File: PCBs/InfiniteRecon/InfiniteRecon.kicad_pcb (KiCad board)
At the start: 4 copper layers, 64 parts, among them J1 USB_C_Receptacle, U1 BQ25185DLHR, U2 MAX17048G_T10, U3 TPS62842DGRR, U4 TPS22918TDBVRQ1, U5 ESP32-S3-WROOM-1, U6 TPL5010DDCR, U7 PCMD3180IRTWR

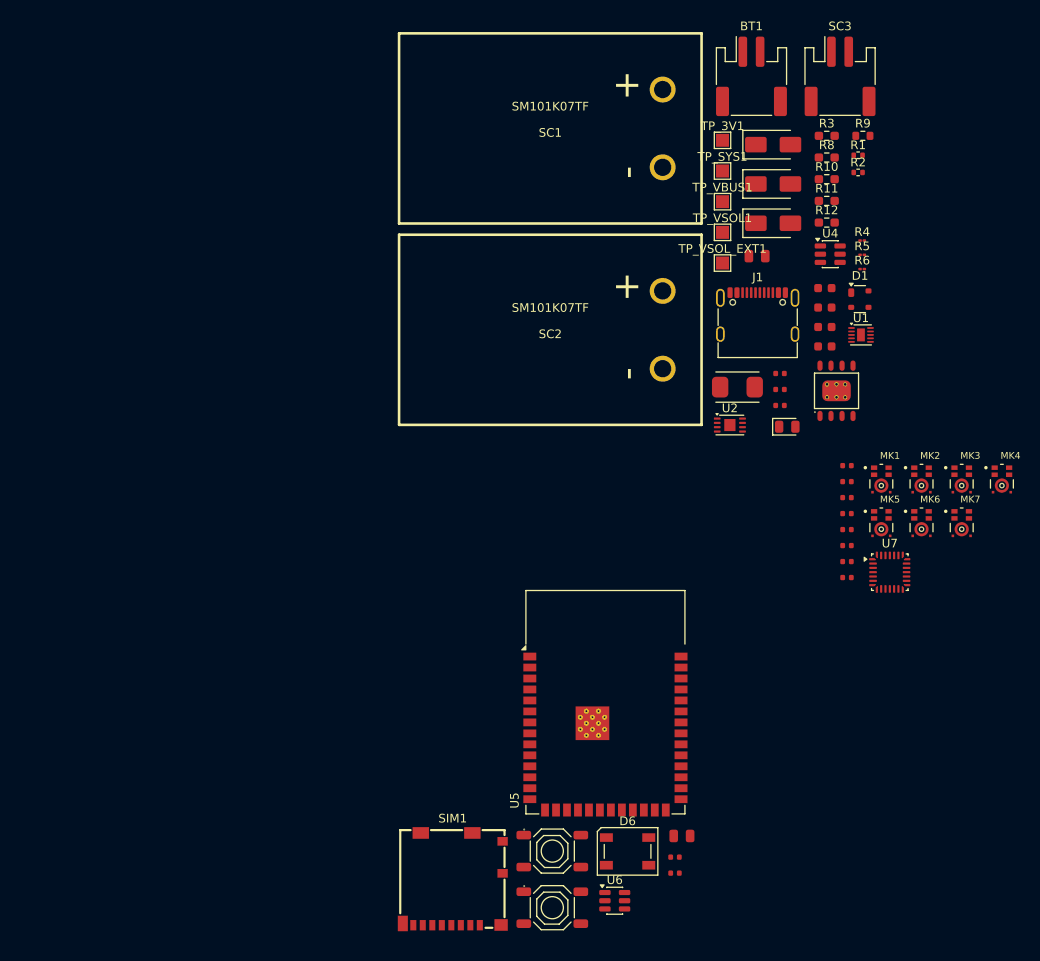
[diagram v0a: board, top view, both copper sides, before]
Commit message: Fixed footprints and some not connected caps
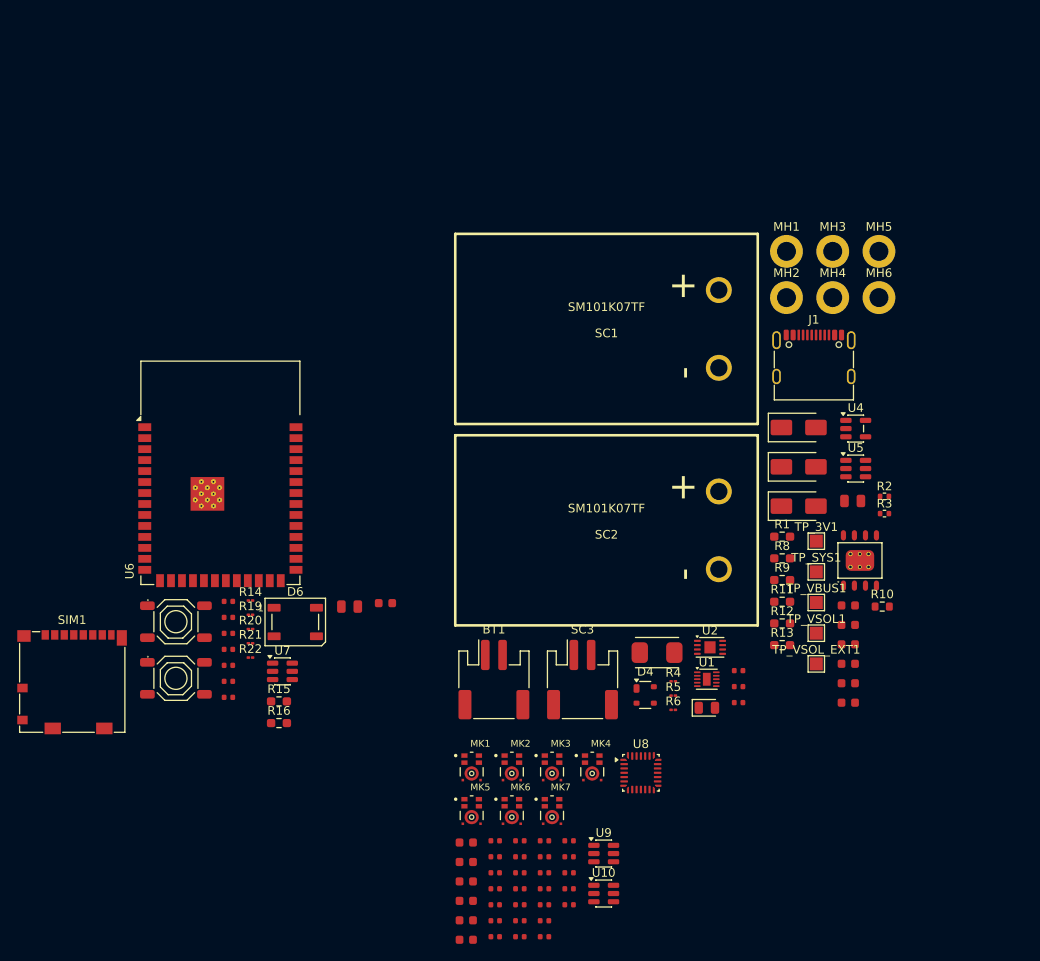
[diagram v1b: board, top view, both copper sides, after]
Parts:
- added C17: 0.1uF, PCM_JLCPCB:C_0402, F.Cu at (156.2, 134.7)
- added C18: 0.1uF, PCM_JLCPCB:C_0402, F.Cu at (156.2, 136.6)
- added C21: 0.1uF, PCM_JLCPCB:C_0402, F.Cu at (156.2, 142.1)
- added C22: 0.1uF, PCM_JLCPCB:C_0402, F.Cu at (156.2, 144.0)
- added C23: 0.1uF, PCM_JLCPCB:C_0402, F.Cu at (156.2, 145.8)
- added C24: 0.1uF, PCM_JLCPCB:C_0402, F.Cu at (159.1, 134.7)
- added C25: 0.1uF, PCM_JLCPCB:C_0402, F.Cu at (159.1, 136.6)
- added C26: 0.1uF, PCM_JLCPCB:C_0402, F.Cu at (159.1, 138.4)
- added C27: 0.1uF, PCM_JLCPCB:C_0402, F.Cu at (159.1, 140.3)
- added C28: 0.1uF, PCM_JLCPCB:C_0402, F.Cu at (159.1, 142.1)
- added C29: 10uF, PCM_JLCPCB:C_0603, F.Cu at (152.9, 134.9)
- added C30: 0.1uF, PCM_JLCPCB:C_0402, F.Cu at (159.1, 144.0)
- added C31: 1uF, PCM_JLCPCB:C_0603, F.Cu at (152.9, 137.2)
- added C32: 1uF, PCM_JLCPCB:C_0603, F.Cu at (152.9, 139.4)
- added C33: 1uF, PCM_JLCPCB:C_0603, F.Cu at (152.9, 141.7)
- added C34: 10uF, PCM_JLCPCB:C_0603, F.Cu at (152.9, 143.9)
- added C35: 0.1uF, PCM_JLCPCB:C_0402, F.Cu at (159.1, 145.8)
- added C36: 10uF, PCM_JLCPCB:C_0603, F.Cu at (152.9, 146.2)
- added C37: 0.1uF, PCM_JLCPCB:C_0402, F.Cu at (161.9, 134.7)
- added MH1: MountingHole_Pad, MountingHole:MountingHole_2.2mm_M2_DIN965_Pad, F.Cu at (189.9, 66.5)
- added MH2: MountingHole_Pad, MountingHole:MountingHole_2.2mm_M2_DIN965_Pad, F.Cu at (189.9, 71.9)
- added MH3: MountingHole_Pad, MountingHole:MountingHole_2.2mm_M2_DIN965_Pad, F.Cu at (195.3, 66.5)
- added MH4: MountingHole_Pad, MountingHole:MountingHole_2.2mm_M2_DIN965_Pad, F.Cu at (195.3, 71.9)
- added MH5: MountingHole_Pad, MountingHole:MountingHole_2.2mm_M2_DIN965_Pad, F.Cu at (200.6, 66.5)
- added MH6: MountingHole_Pad, MountingHole:MountingHole_2.2mm_M2_DIN965_Pad, F.Cu at (200.6, 71.9)
- added R13: 0Ω, Resistor_SMD:R_0603_1608Metric_Pad0.98x0.95mm_HandSolder, F.Cu at (189.4, 112.1)
- added R14: 10K, Resistor_SMD:R_01005_0402Metric, F.Cu at (127.9, 106.9)
- added R15: 10K, Resistor_SMD:R_0603_1608Metric_Pad0.98x0.95mm_HandSolder, F.Cu at (131.2, 118.6)
- added R16: 10K, Resistor_SMD:R_0603_1608Metric_Pad0.98x0.95mm_HandSolder, F.Cu at (131.2, 121.1)
- added R17: 20kΩ, PCM_JLCPCB:R_0402, F.Cu at (125.3, 116.3)
- added R18: 100K, PCM_JLCPCB:R_0402, F.Cu at (125.3, 118.1)
- added R19: 10K, Resistor_SMD:R_01005_0402Metric, F.Cu at (127.9, 108.6)
- added R20: 10K, Resistor_SMD:R_01005_0402Metric, F.Cu at (127.9, 110.2)
- added R21: 10K, Resistor_SMD:R_01005_0402Metric, F.Cu at (127.9, 111.9)
- added R22: 10K, Resistor_SMD:R_01005_0402Metric, F.Cu at (127.9, 113.5)
- added R23: 33, PCM_JLCPCB:R_0402, F.Cu at (161.9, 136.6)
- added R24: 33, PCM_JLCPCB:R_0402, F.Cu at (161.9, 138.4)
- added R25: 33, PCM_JLCPCB:R_0402, F.Cu at (161.9, 140.3)
- added R26: 33, PCM_JLCPCB:R_0402, F.Cu at (161.9, 142.1)
- added R27: 33, PCM_JLCPCB:R_0402, F.Cu at (161.9, 144.0)
- added R28: 33, PCM_JLCPCB:R_0402, F.Cu at (161.9, 145.8)
- added R29: 33, PCM_JLCPCB:R_0402, F.Cu at (164.8, 134.7)
- added R30: 33, PCM_JLCPCB:R_0402, F.Cu at (164.8, 136.6)
- added R31: 33, PCM_JLCPCB:R_0402, F.Cu at (164.8, 138.4)
- added R32: 33, PCM_JLCPCB:R_0402, F.Cu at (164.8, 140.3)
- added R33: 33, PCM_JLCPCB:R_0402, F.Cu at (164.8, 142.1)
- added U10: SN74LVC1T45DBV, Package_TO_SOT_SMD:SOT-23-6, F.Cu at (168.8, 140.8)
- added U8: PCMD3180IRTWR, Package_DFN_QFN:QFN-28_4x4mm_P0.5mm, F.Cu at (173.1, 126.9)
- added U9: SN74LVC1T45DBV, Package_TO_SOT_SMD:SOT-23-6, F.Cu at (168.8, 136.2)
- C11: value 0.1uF -> 1uF; footprint PCM_JLCPCB:C_0402 -> PCM_JLCPCB:C_0603
- C13: value 0.1uF -> 22uF; footprint PCM_JLCPCB:C_0402 -> PCM_JLCPCB:C_0805
- C15: value 22uF -> 0.1uF; footprint PCM_JLCPCB:C_0805 -> PCM_JLCPCB:C_0402
- C20: value 10uF -> 0.1uF; footprint PCM_JLCPCB:C_0603 -> PCM_JLCPCB:C_0402
- C6: value 220pF -> 1uF; footprint PCM_JLCPCB:C_0402 -> PCM_JLCPCB:C_0603
- C7: value 0.1uF -> 220pF
- C8, C9: value 0.1uF -> 10uF; footprint PCM_JLCPCB:C_0402 -> PCM_JLCPCB:C_0603
- D1: value PRTR5V0U2X -> SS14; footprint Package_TO_SOT_SMD:SOT-143 -> PCM_JLCPCB:D_SMA
- D4: value SS14 -> PRTR5V0U2X; footprint PCM_JLCPCB:D_SMA -> Package_TO_SOT_SMD:SOT-143
- D6: value Inolux_IN-PI554FCH -> WS2812B; footprint LED_SMD:LED_Inolux_IN-PI554FCH_PLCC4_5.0x5.0mm_P3.2mm -> LED_SMD:LED_WS2812B_PLCC4_5.0x5.0mm_P3.2mm
- R1: value 5.1K -> 0Ω; footprint Resistor_SMD:R_0402_1005Metric -> Resistor_SMD:R_0603_1608Metric_Pad0.98x0.95mm_HandSolder
- R10: value 0Ω -> 267; footprint Resistor_SMD:R_0603_1608Metric_Pad0.98x0.95mm_HandSolder -> Resistor_SMD:R_0603_1608Metric
- R3: value 0Ω -> 5.1K; footprint Resistor_SMD:R_0603_1608Metric_Pad0.98x0.95mm_HandSolder -> Resistor_SMD:R_0402_1005Metric
- R9: value 267 -> 0Ω; footprint Resistor_SMD:R_0603_1608Metric -> Resistor_SMD:R_0603_1608Metric_Pad0.98x0.95mm_HandSolder
- S1: value BOOT -> RESET
- S2: value RESET -> BOOT
- SIM1: footprint JLCImport:1040310811 -> Connector_Card:microSD_HC_Molex_104031-0811
- U4: value TPS22918TDBVRQ1 -> TLV70018; footprint Package_TO_SOT_SMD:SOT-23-6 -> Package_TO_SOT_SMD:SOT-23-5
- U5: value ESP32-S3-WROOM-1 -> TPS22918TDBVRQ1; footprint RF_Module:ESP32-S3-WROOM-1 -> Package_TO_SOT_SMD:SOT-23-6
- U6: value TPL5010DDCR -> ESP32-S3-WROOM-1; footprint Package_TO_SOT_SMD:SOT-23-6 -> RF_Module:ESP32-S3-WROOM-1
- U7: value PCMD3180IRTWR -> TPL5010DDCR; footprint Package_DFN_QFN:QFN-28_4x4mm_P0.5mm -> Package_TO_SOT_SMD:SOT-23-6
- moved BT1 75.9 mm to (156.1, 116.1)
- moved SC3 75.9 mm to (166.3, 116.1)
- moved C20 73.4 mm to (156.2, 140.3)
- moved C10 72.3 mm to (125.3, 107.0)
- moved C12 72.1 mm to (125.3, 108.9)
- moved U7 71.2 mm to (131.6, 115.1)
- moved U6 67.3 mm to (124.4, 92.1)
- moved MK1 57.9 mm to (153.5, 126.2)
- moved MK2 57.9 mm to (158.1, 126.2)
- moved MK3 57.9 mm to (162.8, 126.2)
- moved MK4 57.9 mm to (167.4, 126.2)
- moved MK5 57.9 mm to (153.5, 131.3)
- moved MK6 57.9 mm to (158.1, 131.3)
- moved MK7 57.9 mm to (162.8, 131.3)
- moved C14 57.8 mm to (125.3, 110.7)
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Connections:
- C10 pad 1: 3V3_SW -> WD_RST
- C11 pad 1: 3V3_SW -> WD_RST
- C12 pad 1: 3V3_SW -> Net-(S2-B)
- C13 pad 1: 3V3_SW -> 3V3
- C19 pad 1: unconnected-(C19-Pad1) -> 1V8
- C19 pad 2: unconnected-(C19-Pad2) -> GND
- C20 pad 1: 3V3_SW -> 1V8
- C6 pad 1: Net-(U4-CT) -> 3V3
- C7 pad 1: 3V3_SW -> Net-(U5-CT)
- C8 pad 1: 3V3 -> 1V8
- D1 pad 1: GND -> Net-(U1-IN)
- D1 pad 2: /Power/USB_D+ -> VBUS
- D2 pad 2: VBUS -> Net-(D2-Pad2)
- D3 pad 2: Net-(D3-Pad2) -> VSOL_EXT
- D4 pad 1: Net-(U1-IN) -> GND
- D4 pad 2: VSOL_EXT -> USB_D+
- D6 pad 1: unconnected-(D6-VSS-Pad1) -> 3V3
- D6 pad 3: unconnected-(D6-VDD-Pad3) -> GND
- D6 pad 4: unconnected-(D6-DO-Pad4) -> NEOPIXEL
- J1 pad A6: /Power/USB_D+ -> USB_D+
- J1 pad A7: /Power/USB_D- -> USB_D-
- J1 pad B6: /Power/USB_D+ -> USB_D+
- J1 pad B7: /Power/USB_D- -> USB_D-
- MK1 pad 1: unconnected-(MK1-DATA-Pad1) -> Net-(MK1-DATA)
- MK1 pad 2: unconnected-(MK1-SELECT-Pad2) -> 1V8
- MK1 pad 3: unconnected-(MK1-GND-Pad3) -> GND
- MK1 pad 6: unconnected-(MK1-CLK-Pad6) -> PDM_CLK_1
- MK1 pad 7: 3V3 -> 1V8
- MK2 pad 1: unconnected-(MK2-DATA-Pad1) -> Net-(MK2-DATA)
- MK2 pad 2: unconnected-(MK2-SELECT-Pad2) -> GND
- MK2 pad 3: unconnected-(MK2-GND-Pad3) -> GND
- MK2 pad 6: unconnected-(MK2-CLK-Pad6) -> PDM_CLK_1
- MK2 pad 7: 3V3_SW -> 1V8
- MK3 pad 1: unconnected-(MK3-DATA-Pad1) -> Net-(MK3-DATA)
- MK3 pad 2: unconnected-(MK3-SELECT-Pad2) -> 1V8
- MK3 pad 3: unconnected-(MK3-GND-Pad3) -> GND
- MK3 pad 6: unconnected-(MK3-CLK-Pad6) -> PDM_CLK_2
- MK3 pad 7: 3V3_SW -> 1V8
- MK4 pad 1: unconnected-(MK4-DATA-Pad1) -> Net-(MK4-DATA)
- MK4 pad 2: unconnected-(MK4-SELECT-Pad2) -> GND
- MK4 pad 3: unconnected-(MK4-GND-Pad3) -> GND
- MK4 pad 6: unconnected-(MK4-CLK-Pad6) -> PDM_CLK_2
- MK4 pad 7: 3V3_SW -> 1V8
- MK5 pad 1: unconnected-(MK5-DATA-Pad1) -> Net-(MK5-DATA)
- MK5 pad 2: unconnected-(MK5-SELECT-Pad2) -> 1V8
- MK5 pad 3: unconnected-(MK5-GND-Pad3) -> GND
- MK5 pad 6: unconnected-(MK5-CLK-Pad6) -> PDM_CLK_3
- MK5 pad 7: 3V3_SW -> 1V8
- MK6 pad 1: unconnected-(MK6-DATA-Pad1) -> Net-(MK6-DATA)
- MK6 pad 2: unconnected-(MK6-SELECT-Pad2) -> GND
- MK6 pad 3: unconnected-(MK6-GND-Pad3) -> GND
- MK6 pad 6: unconnected-(MK6-CLK-Pad6) -> PDM_CLK_3
- MK6 pad 7: 3V3_SW -> 1V8
- MK7 pad 1: unconnected-(MK7-DATA-Pad1) -> Net-(MK7-DATA)
- MK7 pad 2: unconnected-(MK7-SELECT-Pad2) -> GND
- MK7 pad 3: unconnected-(MK7-GND-Pad3) -> GND
- MK7 pad 4: unconnected-(MK7-WAKE-Pad4) -> Net-(MK7-WAKE)
- MK7 pad 5: unconnected-(MK7-THSEL-Pad5) -> 1V8
- MK7 pad 6: unconnected-(MK7-CLK-Pad6) -> PDM_CLK_4
- MK7 pad 7: 3V3_SW -> 1V8
- R1 pad 1: Net-(J1-CC1) -> VSOl
- R1 pad 2: GND -> Net-(D2-Pad2)
- R10 pad 1: Net-(U3-VOS) -> Net-(U3-VSET)
- R10 pad 2: 3V3 -> GND
- R11 pad 1: 3V3_SW -> Net-(U3-VOS)
- R11 pad 2: Net-(U4-VOUT) -> 3V3
- R12 pad 1: Net-(U1-SYS) -> 1V8
- R12 pad 2: SYS -> Net-(U4-OUT)
- R2 pad 1: Net-(J1-CC2) -> Net-(J1-CC1)
- R3 pad 1: VSOL -> Net-(J1-CC2)
- R3 pad 2: Net-(D3-Pad2) -> GND
- R8 pad 1: VBAT -> Net-(U1-SYS)
- R8 pad 2: Net-(U1-BAT) -> SYS
- R9 pad 1: Net-(U3-VSET) -> VBAT
- R9 pad 2: GND -> Net-(U1-BAT)
- S1 pad 1: unconnected-(S1-A-Pad1) -> GND
- S1 pad 2: unconnected-(S1-B-Pad2) -> WD_RST
- S1 pad 3: unconnected-(S1-C-Pad3) -> GND
- S1 pad 4: unconnected-(S1-D-Pad4) -> WD_RST
- S2 pad 1: unconnected-(S2-A-Pad1) -> GND
- S2 pad 2: unconnected-(S2-B-Pad2) -> Net-(S2-B)
- S2 pad 3: unconnected-(S2-C-Pad3) -> GND
- S2 pad 4: unconnected-(S2-D-Pad4) -> Net-(S2-B)
- SC1 pad 1: VSOL -> VSOl
- SIM1 pad 1: unconnected-(SIM1-DAT2-Pad1) -> Net-(SIM1-DAT2)
- SIM1 pad 2: unconnected-(SIM1-DAT3/CD-Pad2) -> CS
- SIM1 pad 3: unconnected-(SIM1-CMD-Pad3) -> MOSI
- SIM1 pad 4: unconnected-(SIM1-VDD-Pad4) -> 3V3_SW
- SIM1 pad 5: unconnected-(SIM1-CLK-Pad5) -> SCK
- SIM1 pad 6: unconnected-(SIM1-VSS-Pad6) -> GND
- SIM1 pad 7: unconnected-(SIM1-DAT0-Pad7) -> MISO
- SIM1 pad 8: unconnected-(SIM1-DAT1-Pad8) -> Net-(SIM1-DAT1)
- U2 pad 5: /Power/BATT_ALERT -> BATT_ALERT
- U2 pad 7: /Power/SCL -> SCL_1
- U2 pad 8: /Power/SDA -> SDA_1
- U4 pad 3: /Power/3V3_SW_EN -> 3V3
- U4 pad 4: Net-(U4-CT) -> unconnected-(U4-NC-Pad4)
- U4 pad 5: unconnected-(U4-QOD-Pad5) -> Net-(U4-OUT)
- U5 pad 1: GND -> 3V3
- U5 pad 2: 3V3 -> GND
- U5 pad 3: unconnected-(U5-EN-Pad3) -> 3V3_SW_EN
- U5 pad 4: unconnected-(U5-IO4-Pad4) -> Net-(U5-CT)
- U5 pad 6: unconnected-(U5-IO6-Pad6) -> Net-(U5-VOUT)
- U6 pad 1: 3V3 -> GND
- U6 pad 2: GND -> 3V3
- U6 pad 3: GND -> WD_RST
- U6 pad 4: unconnected-(U6-DONE-Pad4) -> SDA_1
- U6 pad 5: unconnected-(U6-WAKE-Pad5) -> SCL_1
- U7 pad 1: unconnected-(U7-AVDD-Pad1) -> 3V3
- U7 pad 2: unconnected-(U7-AREG-Pad2) -> GND
- U7 pad 3: unconnected-(U7-VREF-Pad3) -> Net-(U7-DELAY/M_RST)
- U7 pad 4: unconnected-(U7-AVSS-Pad4) -> WD_FEED
- U7 pad 5: unconnected-(U7-MICBIAS-Pad5) -> WD_WAKE
- U7 pad 6: unconnected-(U7-PDMDIN1_GPI1-Pad6) -> WD_RST

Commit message: Finished scem
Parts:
- removed BT1: Battery, Connector_JST:JST_PH_S2B-PH-SM4-TB_1x02-1MP_P2.00mm_Horizontal
- removed C1, C11, C3, C31, C32, C33, C6: 1uF, PCM_JLCPCB:C_0603
- removed C10, C12, C14, C15, C16, C17, C18, C19, C2, C20, C21, C22, C23, C24, C25, C26, C27, C28, C30, C35, C37: 0.1uF, PCM_JLCPCB:C_0402
- removed C13, C5: 22uF, PCM_JLCPCB:C_0805
- removed C29, C34, C36, C4, C8, C9: 10uF, PCM_JLCPCB:C_0603
- removed C7: 220pF, PCM_JLCPCB:C_0402
- removed D1, D2, D3: SS14, PCM_JLCPCB:D_SMA
- removed D4: PRTR5V0U2X, Package_TO_SOT_SMD:SOT-143
- removed D5: CHRG_LED, PCM_JLCPCB:D_0805
- removed D6: WS2812B, LED_SMD:LED_WS2812B_PLCC4_5.0x5.0mm_P3.2mm
- removed J1: USB_C_Receptacle, Connector_USB:USB_C_Receptacle_G-Switch_GT-USB-7010ASV
- removed L1: 2.2uH, PCM_JLCPCB:OSC-SMD_L5.0-W3.2
- removed MH1, MH2, MH3, MH4, MH5, MH6: MountingHole_Pad, MountingHole:MountingHole_2.2mm_M2_DIN965_Pad
- removed MK1, MK2, MK3, MK4, MK5, MK6, MK7: T5838, T5838:MIC_T5838
- removed R1, R11, R12, R13, R8, R9: 0Ω, Resistor_SMD:R_0603_1608Metric_Pad0.98x0.95mm_HandSolder
- removed R10: 267, Resistor_SMD:R_0603_1608Metric
- removed R14, R19, R20, R21, R22, R6: 10K, Resistor_SMD:R_01005_0402Metric
- removed R15, R16: 10K, Resistor_SMD:R_0603_1608Metric_Pad0.98x0.95mm_HandSolder
- removed R17: 20kΩ, PCM_JLCPCB:R_0402
- removed R18: 100K, PCM_JLCPCB:R_0402
- removed R2, R3: 5.1K, Resistor_SMD:R_0402_1005Metric
- removed R23, R24, R25, R26, R27, R28, R29, R30, R31, R32, R33: 33, PCM_JLCPCB:R_0402
- removed R4: 18K, Resistor_SMD:R_01005_0402Metric
- removed R5: 600, Resistor_SMD:R_01005_0402Metric
- removed R7: 1K, PCM_JLCPCB:R_0402
- removed S1: RESET, PCM_JLCPCB:SW-SMD_4P-L5.1-W5.1-P3.70-LS6.5-TL-2
- removed S2: BOOT, PCM_JLCPCB:SW-SMD_4P-L5.1-W5.1-P3.70-LS6.5-TL-2
- removed SC1, SC2: SM101K07TF, ssi_solarcell:SM101K07TF
- removed SC3: External Solar, Connector_JST:JST_PH_S2B-PH-SM4-TB_1x02-1MP_P2.00mm_Horizontal
- removed SIM1: 1040310811, Connector_Card:microSD_HC_Molex_104031-0811
- removed TP_3V1, TP_SYS1, TP_VBUS1, TP_VSOL1, TP_VSOL_EXT1: TestPoint, TestPoint:TestPoint_Pad_1.5x1.5mm
- removed U1: BQ25185DLHR, Package_DFN_QFN:Texas_DLH0010A_WSON-10-1EP_2.2x2mm_P0.4mm_EP0.9x1.5mm
- removed U10, U9: SN74LVC1T45DBV, Package_TO_SOT_SMD:SOT-23-6
- removed U2: MAX17048G_T10, Package_DFN_QFN:TDFN-8-1EP_3x2mm_P0.5mm_EP1.3x1.4mm
- removed U3: TPS62842DGRR, PCM_JLCPCB:ESOP-8_L4.9-W3.9-P1.27-LS6.0-BL-EP
- removed U4: TLV70018, Package_TO_SOT_SMD:SOT-23-5
- removed U5: TPS22918TDBVRQ1, Package_TO_SOT_SMD:SOT-23-6
- removed U6: ESP32-S3-WROOM-1, RF_Module:ESP32-S3-WROOM-1
- removed U7: TPL5010DDCR, Package_TO_SOT_SMD:SOT-23-6
- removed U8: PCMD3180IRTWR, Package_DFN_QFN:QFN-28_4x4mm_P0.5mm

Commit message: Added Mics
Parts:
- added BT1: Battery, Connector_JST:JST_PH_S2B-PH-SM4-TB_1x02-1MP_P2.00mm_Horizontal, F.Cu at (237.7, 65.6)
- added C1: 0.1uF, PCM_JLCPCB:C_0402, F.Cu at (254.4, 60.9)
- added C10: 1uF, PCM_JLCPCB:C_0603, F.Cu at (270.8, 52.0)
- added C11: 220pF, PCM_JLCPCB:C_0402, F.Cu at (254.4, 68.3)
- added C12: 10uF, PCM_JLCPCB:C_0603, F.Cu at (270.8, 54.2)
- added C13: 10uF, PCM_JLCPCB:C_0603, F.Cu at (270.8, 56.5)
- added C14: 1uF, PCM_JLCPCB:C_0603, F.Cu at (270.8, 58.7)
- added C15: 10uF, PCM_JLCPCB:C_0603, F.Cu at (270.8, 61.0)
- added C16: 0.1uF, PCM_JLCPCB:C_0402, F.Cu at (197.6, 56.6)
- added C17: 1uF, PCM_JLCPCB:C_0603, F.Cu at (217.5, 66.4)
- added C18: 0.1uF, PCM_JLCPCB:C_0402, F.Cu at (197.6, 58.4)
- added C19: 22uF, PCM_JLCPCB:C_0805, F.Cu at (217.8, 63.8)
- added C2: 0.1uF, PCM_JLCPCB:C_0402, F.Cu at (254.4, 62.8)
- added C20: 0.1uF, PCM_JLCPCB:C_0402, F.Cu at (197.6, 60.3)
- added C21: 0.1uF, PCM_JLCPCB:C_0402, F.Cu at (197.6, 62.1)
- added C22: 0.1uF, PCM_JLCPCB:C_0402, F.Cu at (197.6, 64.0)
- added C23: 0.1uF, PCM_JLCPCB:C_0402, F.Cu at (233.9, 84.3)
- added C24: 0.1uF, PCM_JLCPCB:C_0402, F.Cu at (233.9, 86.1)
- added C25: 0.1uF, PCM_JLCPCB:C_0402, F.Cu at (233.9, 88.0)
- added C26: 0.1uF, PCM_JLCPCB:C_0402, F.Cu at (233.9, 89.8)
- added C27: 0.1uF, PCM_JLCPCB:C_0402, F.Cu at (233.9, 91.7)
- added C28: 0.1uF, PCM_JLCPCB:C_0402, F.Cu at (233.9, 93.5)
- added C29: 0.1uF, PCM_JLCPCB:C_0402, F.Cu at (236.8, 84.3)
- added C3: 1uF, PCM_JLCPCB:C_0603, F.Cu at (270.8, 43.0)
- added C30: 0.1uF, PCM_JLCPCB:C_0402, F.Cu at (236.8, 86.1)
- added C31: 0.1uF, PCM_JLCPCB:C_0402, F.Cu at (236.8, 88.0)
- added C32: 0.1uF, PCM_JLCPCB:C_0402, F.Cu at (236.8, 89.8)
- added C33: 0.1uF, PCM_JLCPCB:C_0402, F.Cu at (236.8, 91.7)
- added C34: 0.1uF, PCM_JLCPCB:C_0402, F.Cu at (236.8, 93.5)
- added C35: 10uF, PCM_JLCPCB:C_0603, F.Cu at (255.5, 84.5)
- added C36: 0.1uF, PCM_JLCPCB:C_0402, F.Cu at (239.7, 84.3)
- added C37: 1uF, PCM_JLCPCB:C_0603, F.Cu at (255.5, 86.7)
- added C38: 1uF, PCM_JLCPCB:C_0603, F.Cu at (255.5, 89.0)
- added C39: 1uF, PCM_JLCPCB:C_0603, F.Cu at (255.5, 91.2)
- added C4: 0.1uF, PCM_JLCPCB:C_0402, F.Cu at (254.4, 64.6)
- added C40: 10uF, PCM_JLCPCB:C_0603, F.Cu at (255.5, 93.5)
- added C41: 0.1uF, PCM_JLCPCB:C_0402, F.Cu at (239.7, 86.1)
- added C42: 10uF, PCM_JLCPCB:C_0603, F.Cu at (255.5, 95.7)
- added C43: 0.1uF, PCM_JLCPCB:C_0402, F.Cu at (239.7, 88.0)
- added C5: 1uF, PCM_JLCPCB:C_0603, F.Cu at (270.8, 45.2)
- added C6: 0.1uF, PCM_JLCPCB:C_0402, F.Cu at (254.4, 66.5)
- added C7: 10uF, PCM_JLCPCB:C_0603, F.Cu at (261.6, 46.6)
- added C8: 22uF, PCM_JLCPCB:C_0805, F.Cu at (279.2, 57.0)
- added C9: 1uF, PCM_JLCPCB:C_0603, F.Cu at (270.8, 49.7)
- added D1: SS14, PCM_JLCPCB:D_SMA, F.Cu at (281.1, 44.1)
- added D2: SS14, PCM_JLCPCB:D_SMA, F.Cu at (281.1, 48.7)
- added D3: SS14, PCM_JLCPCB:D_SMA, F.Cu at (281.1, 53.2)
- added D4: PRTR5V0U2X, Package_TO_SOT_SMD:SOT-143, F.Cu at (265.3, 67.4)
- added D5: CHRG_LED, PCM_JLCPCB:D_0805, F.Cu at (278.2, 39.5)
- added D6: WS2812B, LED_SMD:LED_WS2812B_PLCC4_5.0x5.0mm_P3.2mm, F.Cu at (-5.15, 0.82)
- added GND1: TestPoint, TestPoint:TestPoint_Pad_1.5x1.5mm, F.Cu at (270.6, 25.9)
- added J1: USB_C_Receptacle, Connector_USB:USB_C_Receptacle_G-Switch_GT-USB-7010ASV, F.Cu at (278.5, 64.8)
- added L1: 2.2uH, PCM_JLCPCB:OSC-SMD_L5.0-W3.2, F.Cu at (259.4, 62.5)
- added MH1: MountingHole_Pad, MountingHole:MountingHole_2.2mm_M2_DIN965_Pad, F.Cu at (271.5, 16.1)
- added MH2: MountingHole_Pad, MountingHole:MountingHole_2.2mm_M2_DIN965_Pad, F.Cu at (271.5, 21.4)
- added MH3: MountingHole_Pad, MountingHole:MountingHole_2.2mm_M2_DIN965_Pad, F.Cu at (276.9, 16.1)
- added MH4: MountingHole_Pad, MountingHole:MountingHole_2.2mm_M2_DIN965_Pad, F.Cu at (276.9, 21.4)
- added MH5: MountingHole_Pad, MountingHole:MountingHole_2.2mm_M2_DIN965_Pad, F.Cu at (282.2, 16.1)
- added MH6: MountingHole_Pad, MountingHole:MountingHole_2.2mm_M2_DIN965_Pad, F.Cu at (282.2, 21.4)
- added MK1: T5838, T5838:MIC_T5838, F.Cu at (27.5, 0.00)
- added MK2: T5838, T5838:MIC_T5838, F.Cu at (13.8, 23.8)
- added MK3: T5838, T5838:MIC_T5838, F.Cu at (-13.8, 23.8)
- added MK4: T5838, T5838:MIC_T5838, F.Cu at (-27.5, 0.00)
- added MK5: T5838, T5838:MIC_T5838, F.Cu at (-13.8, -23.8)
- added MK6: T5838, T5838:MIC_T5838, F.Cu at (13.8, -23.8)
- added MK7: T5838, T5838:MIC_T5838, F.Cu at (0.00, 0.00)
- added R1: 0Ω, Resistor_SMD:R_0603_1608Metric_Pad0.98x0.95mm_HandSolder, F.Cu at (274.9, 43.1)
- added R10: 267, Resistor_SMD:R_0603_1608Metric, F.Cu at (283.5, 56.8)
- added R11: 0Ω, Resistor_SMD:R_0603_1608Metric_Pad0.98x0.95mm_HandSolder, F.Cu at (274.9, 50.6)
- added R12: 100K, PCM_JLCPCB:R_0402, F.Cu at (254.4, 70.2)
- added R13: 0Ω, Resistor_SMD:R_0603_1608Metric_Pad0.98x0.95mm_HandSolder, F.Cu at (274.9, 53.1)
- added R14: 0Ω, Resistor_SMD:R_0603_1608Metric_Pad0.98x0.95mm_HandSolder, F.Cu at (274.9, 55.7)
- added R15: 0Ω, Resistor_SMD:R_0603_1608Metric_Pad0.98x0.95mm_HandSolder, F.Cu at (274.9, 58.2)
- added R16: 10K, Resistor_SMD:R_0402_1005Metric, F.Cu at (214.2, 56.6)
- added R17: 100K, PCM_JLCPCB:R_0402, F.Cu at (197.6, 65.8)
- added R18: 10K, Resistor_SMD:R_0603_1608Metric_Pad0.98x0.95mm_HandSolder, F.Cu at (210.5, 56.9)
- added R19: 10K, Resistor_SMD:R_0603_1608Metric_Pad0.98x0.95mm_HandSolder, F.Cu at (210.5, 59.4)
- added R2: 5.1K, Resistor_SMD:R_0402_1005Metric, F.Cu at (282.5, 25.1)
- added R20: 10K, Resistor_SMD:R_0603_1608Metric_Pad0.98x0.95mm_HandSolder, F.Cu at (210.5, 61.9)
- added R21: 10K, Resistor_SMD:R_0603_1608Metric_Pad0.98x0.95mm_HandSolder, F.Cu at (210.5, 64.4)
- added R22: 10K, Resistor_SMD:R_0603_1608Metric_Pad0.98x0.95mm_HandSolder, F.Cu at (210.5, 66.9)
- added R23: 20kΩ, PCM_JLCPCB:R_0402, F.Cu at (197.6, 67.7)
- added R24: 100K, PCM_JLCPCB:R_0402, F.Cu at (197.6, 69.5)
- added R25: 10K, Resistor_SMD:R_0402_1005Metric, F.Cu at (214.2, 58.6)
- added R26: 10K, Resistor_SMD:R_0402_1005Metric, F.Cu at (214.2, 60.6)
- added R27: 10K, Resistor_SMD:R_0402_1005Metric, F.Cu at (214.2, 62.6)
- added R28: 10K, Resistor_SMD:R_0402_1005Metric, F.Cu at (214.2, 64.6)
- added R29: 33, Resistor_SMD:R_0402_1005Metric, F.Cu at (249.2, 84.3)
- added R3: 5.1K, Resistor_SMD:R_0402_1005Metric, F.Cu at (282.5, 27.1)
- added R30: 33, Resistor_SMD:R_0402_1005Metric, F.Cu at (249.2, 86.3)
- added R31: 33, Resistor_SMD:R_0402_1005Metric, F.Cu at (249.2, 88.3)
- added R32: 33, Resistor_SMD:R_0402_1005Metric, F.Cu at (249.2, 90.3)
- added R33: 33, Resistor_SMD:R_0402_1005Metric, F.Cu at (249.2, 92.3)
- added R34: 33, Resistor_SMD:R_0402_1005Metric, F.Cu at (249.2, 94.3)
- added R35: 33, Resistor_SMD:R_0402_1005Metric, F.Cu at (252.1, 84.3)
- added R36: 33, Resistor_SMD:R_0402_1005Metric, F.Cu at (252.1, 86.3)
- added R37: 33, Resistor_SMD:R_0402_1005Metric, F.Cu at (252.1, 88.3)
- added R38: 33, Resistor_SMD:R_0402_1005Metric, F.Cu at (252.1, 90.3)
- added R39: 33, Resistor_SMD:R_0402_1005Metric, F.Cu at (252.1, 92.3)
- added R4: 600, Resistor_SMD:R_0402_1005Metric, F.Cu at (282.5, 29.1)
- added R5: 18k, Resistor_SMD:R_0402_1005Metric, F.Cu at (282.5, 31.1)
- added R6: 10K, Resistor_SMD:R_0402_1005Metric, F.Cu at (282.5, 33.1)
- added R7: 1K, Resistor_SMD:R_0402_1005Metric, F.Cu at (282.5, 35.0)
- added R8: 0Ω, Resistor_SMD:R_0603_1608Metric_Pad0.98x0.95mm_HandSolder, F.Cu at (274.9, 45.6)
- added R9: 0Ω, Resistor_SMD:R_0603_1608Metric_Pad0.98x0.95mm_HandSolder, F.Cu at (274.9, 48.1)
- added S1: RESET, PCM_JLCPCB:SW-SMD_4P-L5.1-W5.1-P3.70-LS6.5-TL-2, F.Cu at (-21.0, 10.5)
- added S2: BOOT, PCM_JLCPCB:SW-SMD_4P-L5.1-W5.1-P3.70-LS6.5-TL-2, F.Cu at (21.1, 10.7)
- added SC1: SM101K07TF, ssi_solarcell:SM101K07TF, B.Cu at (-65.5, 7.67)
- added SC2: SM101K07TF, ssi_solarcell:SM101K07TF, B.Cu at (-65.7, 31.3)
- added SC3: External Solar, Connector_JST:JST_PH_S2B-PH-SM4-TB_1x02-1MP_P2.00mm_Horizontal, F.Cu at (247.9, 65.6)
- added SIM1: 1040310811, Connector_Card:microSD_HC_Molex_104031-0811, F.Cu at (24.8, 132.5)
- added TP_1V1: TestPoint, TestPoint:TestPoint_Pad_1.5x1.5mm, F.Cu at (270.6, 29.4)
- added TP_1V2: TestPoint, TestPoint:TestPoint_Pad_1.5x1.5mm, F.Cu at (270.6, 33.0)
- added TP_1V8_SW1: TestPoint, TestPoint:TestPoint_Pad_1.5x1.5mm, F.Cu at (270.6, 36.5)
- added TP_3V1: TestPoint, TestPoint:TestPoint_Pad_1.5x1.5mm, F.Cu at (270.6, 40.1)
- added TP_3V3_SW1: TestPoint, TestPoint:TestPoint_Pad_1.5x1.5mm, F.Cu at (274.1, 25.9)
- added TP_SYS1: TestPoint, TestPoint:TestPoint_Pad_1.5x1.5mm, F.Cu at (274.1, 29.4)
- added TP_VBUS1: TestPoint, TestPoint:TestPoint_Pad_1.5x1.5mm, F.Cu at (274.1, 33.0)
- added TP_VSOL1: TestPoint, TestPoint:TestPoint_Pad_1.5x1.5mm, F.Cu at (274.1, 36.5)
- added TP_VSOL_EXT1: TestPoint, TestPoint:TestPoint_Pad_1.5x1.5mm, F.Cu at (274.1, 40.1)
- added U1: BQ25185DLHR, Package_DFN_QFN:Texas_DLH0010A_WSON-10-1EP_2.2x2mm_P0.4mm_EP0.9x1.5mm, F.Cu at (265.1, 61.9)
- added U10: SN74LVC1T45DBV, Package_TO_SOT_SMD:SOT-23-6, F.Cu at (253.7, 75.7)
- added U11: SN74LVC1T45DBV, Package_TO_SOT_SMD:SOT-23-6, F.Cu at (253.7, 80.3)
- added U2: MAX17048G_T10, Package_DFN_QFN:DFN-8-1EP_2x2mm_P0.5mm_EP0.9x1.3mm, F.Cu at (283.2, 37.9)
- added U3: TPS62842DGRR, Package_SO:HVSSOP-8-1EP_3x3mm_P0.65mm_EP1.57x1.89mm_ThermalVias, F.Cu at (259.5, 67.4)
- added U4: TLV70018, Package_TO_SOT_SMD:SOT-23-5, F.Cu at (278.5, 26.5)
- added U5: TPS22918TDBVRQ1, Package_TO_SOT_SMD:SOT-23-6, F.Cu at (278.5, 31.1)
- added U6: TLV70018, Package_TO_SOT_SMD:SOT-23-5, F.Cu at (278.5, 35.8)
- added U7: ESP32-S3-WROOM-1, RF_Module:ESP32-S3-WROOM-1, F.Cu at (-0.40, 22.8)
- added U8: TPL5010DDCR, Package_TO_SOT_SMD:SOT-23-6, F.Cu at (226.3, 58.0)
- added U9: PCMD3180IRTWR, Package_DFN_QFN:WQFN-24-1EP_4x4mm_P0.5mm_EP2.45x2.45mm_ThermalVias, F.Cu at (244.6, 86.5)
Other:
- board outline added: 60 x 60 mm

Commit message: lots of routing to be done
maybe its time to descope...
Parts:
- removed GND1: TestPoint, TestPoint:TestPoint_Pad_1.5x1.5mm
- removed MH4, MH5, MH6: MountingHole_Pad, MountingHole:MountingHole_2.2mm_M2_DIN965_Pad
- removed R39: 33, Resistor_SMD:R_0402_1005Metric
- added J2: Conn_01x04_Pin, Connector_JST:JST_GH_SM04B-GHS-TB_1x04-1MP_P1.25mm_Horizontal, F.Cu at (-18.7, 19.2)
- J1: footprint Connector_USB:USB_C_Receptacle_G-Switch_GT-USB-7010ASV -> Connector_USB:USB_C_Receptacle_GCT_USB4110
- R12, R17, R23: footprint PCM_JLCPCB:R_0402 -> Resistor_SMD:R_0402_1005Metric
- R24: value 100K -> 10K; footprint PCM_JLCPCB:R_0402 -> Resistor_SMD:R_0402_1005Metric
- R28: value 10K -> 33
- S1: value RESET -> Tactile Button, 160gf; footprint PCM_JLCPCB:SW-SMD_4P-L5.1-W5.1-P3.70-LS6.5-TL-2 -> PCM_JLCPCB:SW_TS-1088-AR02016
- S2: value BOOT -> Tactile Button, 160gf; footprint PCM_JLCPCB:SW-SMD_4P-L5.1-W5.1-P3.70-LS6.5-TL-2 -> PCM_JLCPCB:SW_TS-1088-AR02016
- moved MH2 298.4 mm to (-26.5, 6.25)
- moved SC3 280.0 mm to (-20.7, -13.5), turned to -165 degrees
- moved MH1 265.6 mm to (9.25, -25.8)
- moved MH3 258.6 mm to (18.2, 20.5)
- moved J1 258.2 mm to (25.8, 12.2)
- moved TP_VSOL1 235.8 mm to (48.5, -31.8)
- moved BT1 232.5 mm to (28.8, -36.6), turned to 165 degrees
- moved TP_1V1 229.3 mm to (51.2, -37.5)
- moved TP_1V2 229.2 mm to (49.0, -25.5)
- moved TP_3V1 228.2 mm to (55.7, -36.6)
- moved TP_3V3_SW1 225.7 mm to (55.8, -31.2)
- moved TP_VBUS1 223.1 mm to (62.2, -36.8)
- moved TP_1V8_SW1 221.9 mm to (57.8, -26.2)
- moved TP_VSOL_EXT1 221.0 mm to (65.2, -32.0)
- moved TP_SYS1 215.0 mm to (66.5, -26.5)
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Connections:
- MK1 pad 2: 1V8 -> 1V8_SW
- MK3 pad 2: 1V8 -> 1V8_SW
- MK5 pad 2: 1V8 -> 1V8_SW
- R24 pad 2: WD_RST -> SCL_1
- R25 pad 2: SCL_1 -> SDA_1
- R26 pad 1: 3V3 -> 3V3_SW
- R26 pad 2: SDA_1 -> SCL_SW
- R27 pad 2: SCL_SW -> SDA_SW
- R28 pad 1: 3V3_SW -> Net-(MK1-DATA)
- R28 pad 2: SDA_SW -> PDM_DIN_1
- R29 pad 1: Net-(MK1-DATA) -> Net-(MK2-DATA)
- R30 pad 1: Net-(MK2-DATA) -> Net-(MK3-DATA)
- R30 pad 2: PDM_DIN_1 -> PDM_DIN_2
- R31 pad 1: Net-(MK3-DATA) -> Net-(MK4-DATA)
- R32 pad 1: Net-(MK4-DATA) -> Net-(MK5-DATA)
- R32 pad 2: PDM_DIN_2 -> PDM_DIN_3
- R33 pad 1: Net-(MK5-DATA) -> Net-(MK6-DATA)
- R34 pad 1: Net-(MK6-DATA) -> PDM_CLK_1
- R34 pad 2: PDM_DIN_3 -> Net-(U9-PDMCLK1_GPO1)
- R35 pad 1: PDM_CLK_1 -> PDM_CLK_2
- R35 pad 2: Net-(U9-PDMCLK1_GPO1) -> Net-(U9-PDMCLK2_GPO2)
- R36 pad 1: PDM_CLK_2 -> PDM_CLK_3
- R36 pad 2: Net-(U9-PDMCLK2_GPO2) -> Net-(U9-PDMCLK3_GPO3)
- R37 pad 1: PDM_CLK_3 -> Net-(MK7-DATA)
- R37 pad 2: Net-(U9-PDMCLK3_GPO3) -> PDM_DIN_4
- R38 pad 1: Net-(MK7-DATA) -> Net-(U9-PDMCLK4_GPO4)
- R38 pad 2: PDM_DIN_4 -> PDM_CLK_4
- U7 pad 36: unconnected-(U7-RXD0-Pad36) -> TX
- U7 pad 37: unconnected-(U7-TXD0-Pad37) -> RX
